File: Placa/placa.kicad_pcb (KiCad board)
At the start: 2 copper layers, 70 x 80 mm, 78 parts, among them IC1 ATMEGA328-A, P1 CONN_01X04, P10 CONN_01X02, P12 CONN_02X03, P2 CONN_01X02, P3 CONN_01X02, P4 BallCaster2, P5 BallCaster1, P6 CONN_01X04, P7 CONN_01X04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

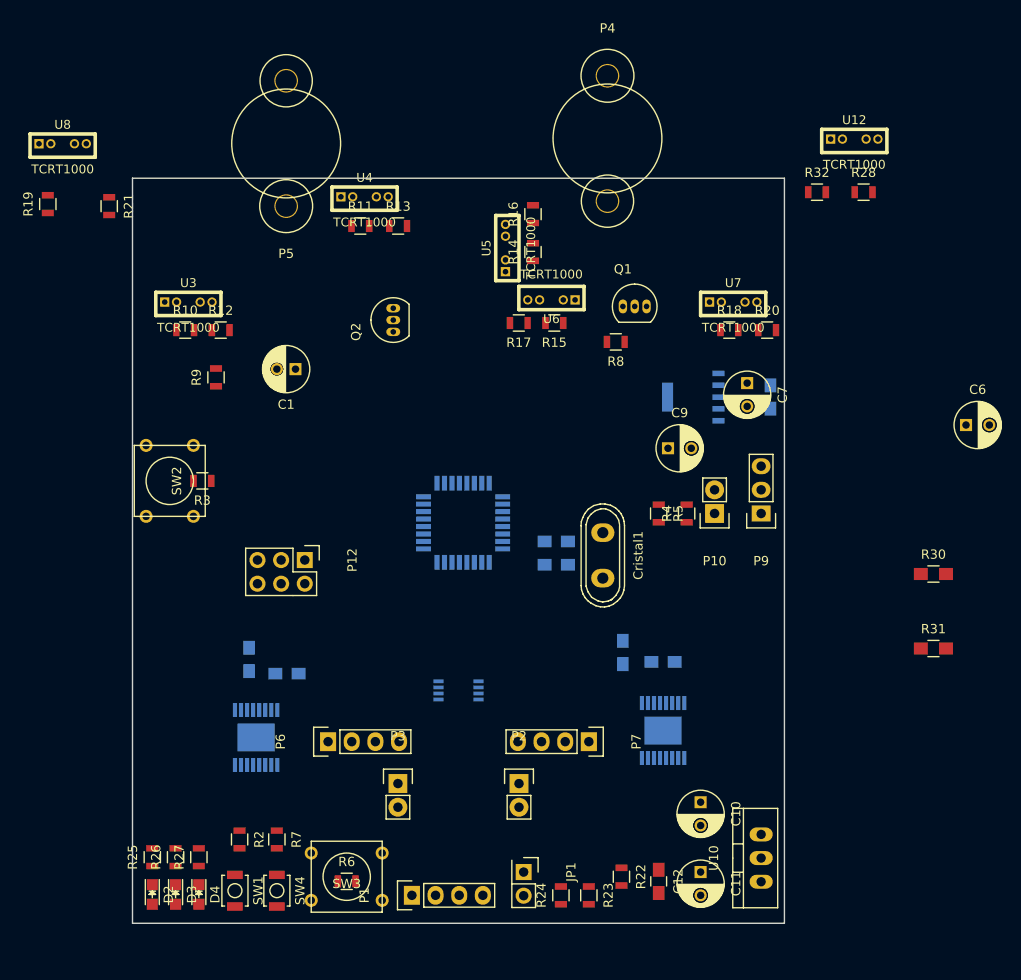
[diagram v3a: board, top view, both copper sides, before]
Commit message: Está todo ruteado, falta engrozar pistas, chequear wiki y un chequeo general
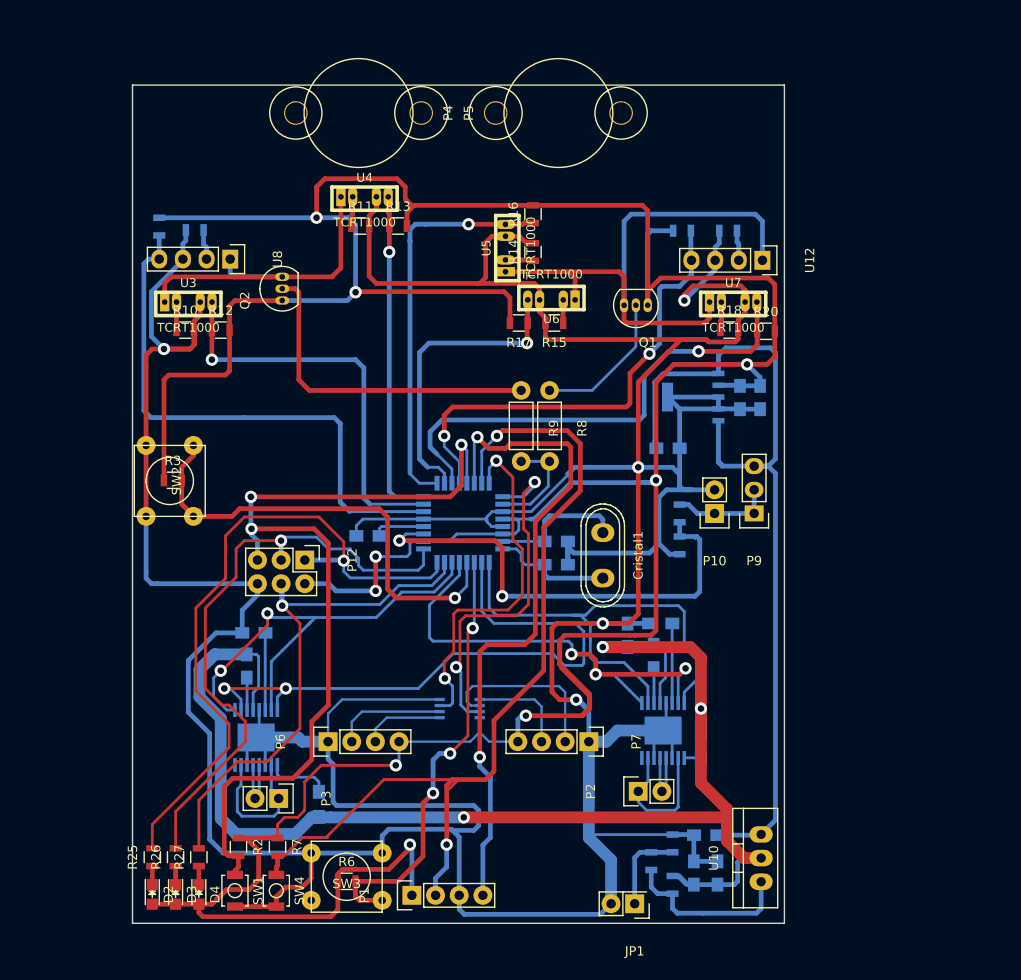
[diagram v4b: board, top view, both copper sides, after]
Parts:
- C1: footprint Capacitors_ThroughHole:C_Radial_D5_L11_P2 -> Capacitors_SMD:C_0805_HandSoldering; moved to B.Cu
- C10, C11, C6, C7, C9: footprint Capacitors_ThroughHole:C_Radial_D5_L11_P2.5 -> Capacitors_SMD:C_0805_HandSoldering; moved to B.Cu
- C12, R19, R21, R22, R23, R24, R28, R30, R31, R32, R4, R5: moved to B.Cu
- R8, R9: footprint Resistors_SMD:R_0805 -> Resistors_ThroughHole:Resistor_Horizontal_RM7mm
- U12, U8: footprint tcrt1000:TCRT1000 -> Pin_Headers:Pin_Header_Straight_1x04
- moved R31 68.1 mm to (120.0, 102.2), turned to 270 degrees
- moved C6 42.8 mm to (153.2, 84.1), turned to 90 degrees
- moved R9 32.8 mm to (141.7, 57.8), turned to 270 degrees
- moved R30 31.0 mm to (161.0, 95.9), turned to 90 degrees
- moved U8 21.7 mm to (110.5, 43.7), turned to 270 degrees
- moved C1 19.5 mm to (125.3, 73.4)
- moved P5 17.6 mm to (131.0, 28.0), turned to 270 degrees
- moved U12 16.2 mm to (167.6, 43.8), turned to 270 degrees
- moved R19 16.0 mm to (106.7, 40.6), turned to 180 degrees
- moved R28 15.1 mm to (164.0, 40.6), turned to 180 degrees
- moved R32 15.1 mm to (159.0, 40.6), turned to 180 degrees
- moved R24 13.2 mm to (158.0, 106.4)
- moved P3 12.9 mm to (115.7, 101.6), turned to 270 degrees
- moved P2 12.8 mm to (154.3, 100.8), turned to 90 degrees
- moved P4 12.6 mm to (139.0, 28.0), turned to 90 degrees
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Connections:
- IC1 pad 1: /EncoderM2 -> /EncoderM1
- IC1 pad 13: /Motores/M2IN1 -> /Motores/M1IN1
- IC1 pad 14: /Motores/M1IN1 -> /Motores/M2IN1
- IC1 pad 32: /EncoderM1 -> /EncoderM2
- R12 pad 1: /Sensores/Sensor1 -> /Sensores/Sensor2
- R13 pad 1: /Sensores/Sensor4 -> /Sensores/Sensor3
- R16 pad 1: /Sensores/Sensor5 -> /Sensores/Sensor4
- R17 pad 1: /Sensores/Sensor2 -> /Sensores/Sensor5
- R20 pad 1: /Sensores/Sensor3 -> /Sensores/Sensor6
- R21 pad 1: /Sensores/Sensor6 -> /Sensores/Sensor1
- R25 pad 2: /Led1 -> /Led2
- R26 pad 2: /Led2 -> /Led3
- R27 pad 2: /Led3 -> /Led1
- U12 pad 1: /Sensores/habilitado2 -> /Sensores/habilitado
- U3 pad 1: /Sensores/habilitado -> /Sensores/habilitado2
- U3 pad 4: /Sensores/Sensor1 -> /Sensores/Sensor2
- U4 pad 4: /Sensores/Sensor4 -> /Sensores/Sensor3
- U5 pad 1: /Sensores/habilitado2 -> /Sensores/habilitado
- U5 pad 4: /Sensores/Sensor5 -> /Sensores/Sensor4
- U6 pad 4: /Sensores/Sensor2 -> /Sensores/Sensor5
- U7 pad 4: /Sensores/Sensor3 -> /Sensores/Sensor6
- U8 pad 4: /Sensores/Sensor6 -> /Sensores/Sensor1
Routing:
- net GND: track 0.00 -> 588.1 mm, vias 0 -> 5
- net +5V: track 0.00 -> 428.1 mm, vias 0 -> 9
- net VPP: track 0.00 -> 158.0 mm, vias 0 -> 3
- net /Alimentacion/Vbat: track 0.00 -> 145.9 mm
- net /Reset: track 0.00 -> 132.0 mm, vias 0 -> 3
- net /BotonExtra: track 0.00 -> 106.3 mm, vias 0 -> 2
- net /Led2: track 0.00 -> 73.5 mm, vias 0 -> 1
- net /RX: track 0.00 -> 71.3 mm, vias 0 -> 2
- net /Led3: track 0.00 -> 69.7 mm, vias 0 -> 1
- net /Motores/M2IN2: track 0.00 -> 67.7 mm, vias 0 -> 2
- net /Sensores/habilitado: track 0.00 -> 62.8 mm
- net /Sensores/Sensor1: track 0.00 -> 60.1 mm
- net /Led1: track 0.00 -> 60.0 mm, vias 0 -> 1
- net /Sensores/Sensor6: track 0.00 -> 59.8 mm, vias 0 -> 1
- net /Boton1: track 0.00 -> 55.6 mm, vias 0 -> 1
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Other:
- board size 70 x 80 mm -> 70 x 90 mm
- net class Default: clearance 0.2 -> 0.3048; trace_width 0.25 -> 0.3048; via_dia 0.6 -> 1.3208; via_drill 0.4 -> 0.7
- rule trace_clearance: 0.2 -> 0.3048

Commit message: Se termino la placa, y se mando a fabricar.
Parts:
- C10, C11, C6, C7, C9: footprint Capacitors_SMD:C_0805_HandSoldering -> Capacitors_SMD:C_1206
- P10: footprint Pin_Headers:Pin_Header_Straight_1x02 -> Connectors_Molex:Molex_KK-6410-02_02x2.54mm_Straight
- moved R6 6.03 mm to (124.5, 104.6)
- moved R3 5.53 mm to (109.9, 67.2)
- moved R4 3.20 mm to (155.6, 71.4)
- moved R5 3.20 mm to (155.6, 74.8)
- moved P10 1.22 mm to (161.3, 70.9), turned to 90 degrees
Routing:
- net +5V: track 428.1 -> 498.3 mm
- net /Alimentacion/Vbat: track 145.9 -> 200.4 mm
- net /Boton2: track 49.5 -> 73.4 mm
- net /Reset: track 132.0 -> 114.6 mm
- net GND: track 588.1 -> 598.7 mm
- net Net-(R22-Pad2): track 18.8 -> 27.2 mm
- net +BATT: track 11.3 -> 18.9 mm
- net /RX: track 71.3 -> 78.7 mm
- net /BatteryControl: track 52.1 -> 45.8 mm
- net VPP: track 158.0 -> 160.9 mm
- net (no net): track 0.00 -> 2.51 mm
- net Net-(JP1-Pad1): track 17.3 -> 19.3 mm
- net /BotonExtra: track 106.3 -> 104.8 mm
- added copper zone on F.Cu, net +5V
- added copper zone on B.Cu, net GND
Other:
- board text added: "Arión"
- board text added: "CDR - FIUBA"

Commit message: Agrego cambios sugeridos en la wiki de github.
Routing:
- added copper zone on F.Cu, net GND
- removed copper zone on F.Cu, net +5V
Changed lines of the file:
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@@
   )
   (setup
-    (last_trace_width 0.508)
+    (last_trace_width 0.3048)
     (user_trace_width 0.254)
     (user_trace_width 0.3048)
@@
   (segment (start 119.507 99.314) (end 115.824 99.314) (width 0.3048) (layer B.Cu) (net 61))
   (segment (start 120.015 99.822) (end 119.507 99.314) (width 0.3048) (layer B.Cu) (net 61))
-  (zone (net 7) (net_name +5V) (layer F.Cu) (hatch edge 0.508)
+  (zone (net 5) (net_name GND) (layer F.Cu) (hatch edge 0.508)
     (connect_pads (clearance 0.508))
     (min_thickness 0.254)
